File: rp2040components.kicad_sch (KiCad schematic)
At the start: 14 parts, among them P2 Header 1.27mm 2x5 PTH, P3 Header 3, U8 W25Q128JVSIQTR, Y1 X322512MSB4SI

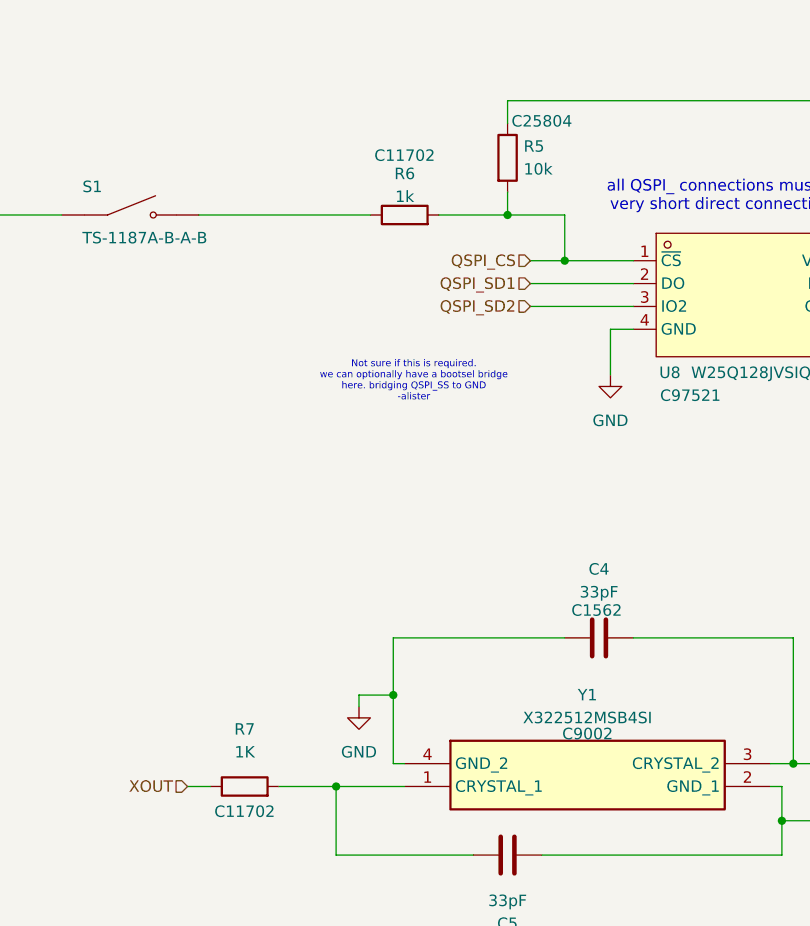
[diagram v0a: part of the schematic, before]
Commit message: Attached part number to components.
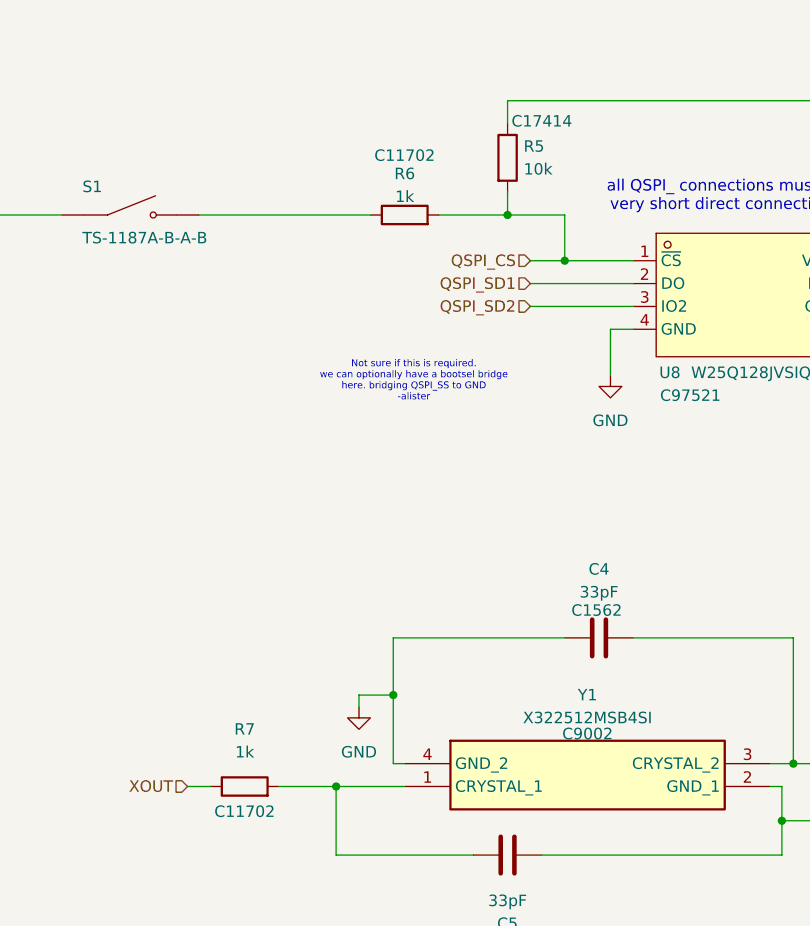
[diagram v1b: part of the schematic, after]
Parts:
- C18: value CL05B104KO5NNNC -> 100nF; footprint Imported Altium Library:CAPC1050X55X23ML05T13 -> Capacitor_SMD:C_0402_1005Metric
- R5: footprint Resistor_SMD:R_0603_1608Metric -> Resistor_SMD:R_0805_2012Metric; LCSC PN C25804 -> C17414
- R7: value 1K -> 1k
- Y1: footprint X322512MSB4SI -> Crystal:Crystal_SMD_TXC_7M-4Pin_3.2x2.5mm
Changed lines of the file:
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@@
 			)
 		)
-		(property "Footprint" "X322512MSB4SI"
+		(property "Footprint" "Crystal:Crystal_SMD_TXC_7M-4Pin_3.2x2.5mm"
 			(at 156.21 204.14 0)
 			(hide yes)
@@
 			)
 		)
-		(property "Footprint" "Resistor_SMD:R_0603_1608Metric"
+		(property "Footprint" "Resistor_SMD:R_0805_2012Metric"
 			(at 129.032 41.91 90)
 			(hide yes)
@@
 			)
 		)
-		(property "LCSC PN" "C25804"
+		(property "LCSC PN" "C17414"
 			(at 134.62 37.846 0)
 			(show_name no)
@@
 			)
 		)
-		(property "Value" "CL05B104KO5NNNC"
+		(property "Value" "100nF"
 			(at 259.08 127 0)
 			(hide yes)
@@
 			)
 		)
-		(property "Footprint" "Imported Altium Library:CAPC1050X55X23ML05T13"
+		(property "Footprint" "Capacitor_SMD:C_0402_1005Metric"
 			(at 255.27 119.38 0)
 			(hide yes)
@@
 			)
 		)
-		(property "Value" "1K"
+		(property "Value" "1k"
 			(at 101.6 107.95 90)
 			(show_name no)

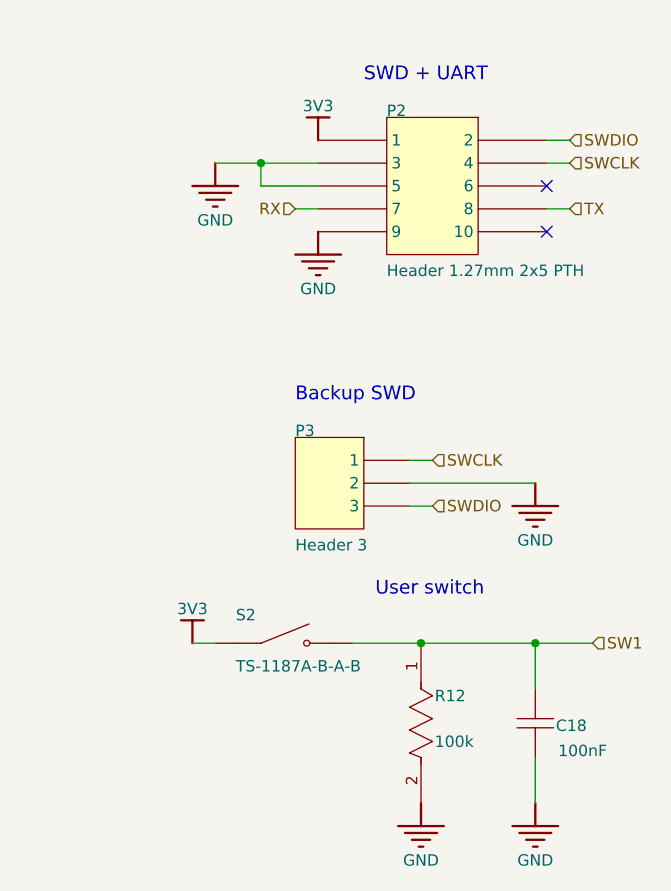
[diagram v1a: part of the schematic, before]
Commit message: Fix ERC errors.
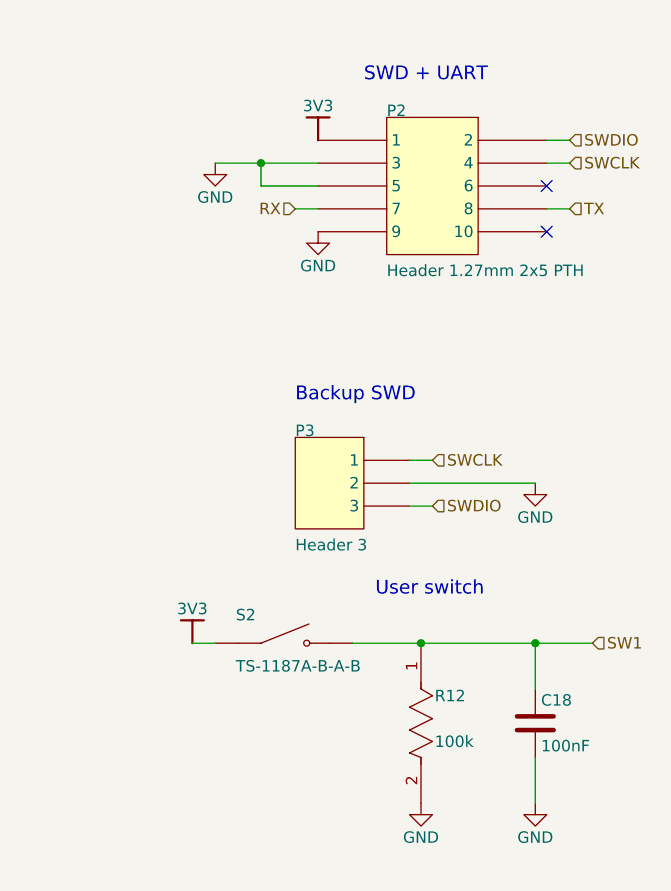
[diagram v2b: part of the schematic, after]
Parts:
- C18: symbol James Cook University:root_1_CAP-NP-2_James Cook University -> Device:C; CAPACITANCE 100nF -> (none); CASE SIZE/DIMENSION 0402 -> (none); DATASHEET URL https://datasheet.ciiva.com/29198/458718-da-01-en-vs-konden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 -> (none); DATASHEET VERSION Nov-10 -> (none); DIELECTRIC X7R -> (none); MANUFACTURER Samsung Electro-Mechanics -> (none); MANUFACTURER URL http://www.samsungsem.com/global/index.jsp -> (none); RATED VOLTAGE 16V -> (none); TOLERANCE (%) ±10% -> (none)
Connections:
- net GND: now also C18.2; no longer C18.1
- net SW1: now also C18.1; no longer C18.2

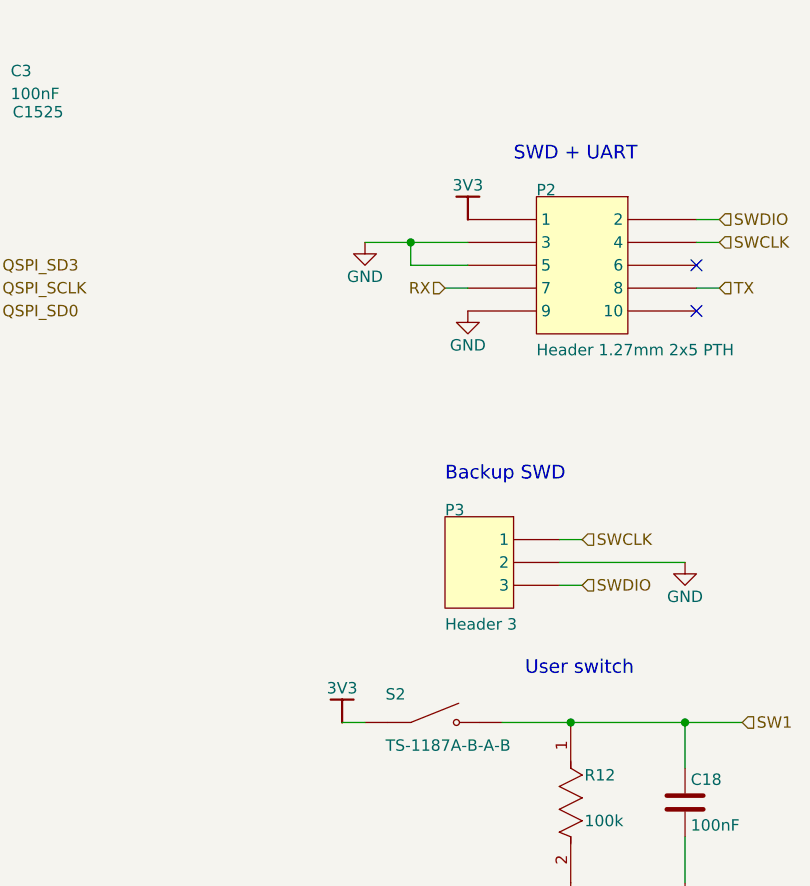
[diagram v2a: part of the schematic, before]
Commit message: Fix ERC errors.
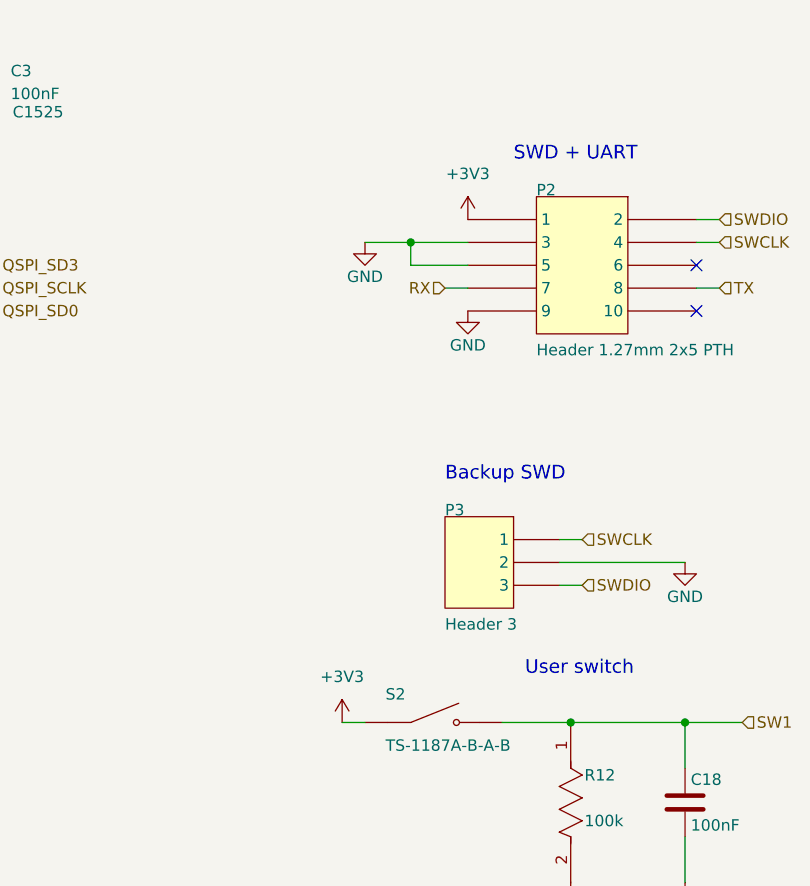
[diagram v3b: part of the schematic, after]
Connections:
- net 3V3 renamed +3V3
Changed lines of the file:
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@@
-	)
-	(symbol
-		(lib_id "CC3501 Assignment 1-altium-import:3V3_BAR")
-		(at 231.14 50.8 180)
-		(unit 1)
-		(body_style 1)
-		(exclude_from_sim no)
-		(in_bom yes)
-		(on_board yes)
-		(in_pos_files yes)
-		(dnp no)
-		(property "Reference" "#PWR0144"
-			(at 231.14 50.8 0)
-			(hide yes)
-			(show_name no)
-			(do_not_autoplace no)
-			(effects
-				(font
-					(size 1.27 1.27)
-				)
-			)
-		)
-		(property "Value" "3V3"
-			(at 231.14 46.99 0)
-			(show_name no)
-			(do_not_autoplace no)
-			(effects
-				(font
-					(size 1.27 1.27)
-				)
-			)
-		)
-		(property "Footprint" ""
-			(at 231.14 50.8 0)
-			(show_name no)
-			(do_not_autoplace no)
-			(effects
-				(font
-					(size 1.27 1.27)
-				)
-			)
-		)
-		(property "Datasheet" ""
-			(at 231.14 50.8 0)
-			(show_name no)
-			(do_not_autoplace no)
-			(effects
-				(font
-					(size 1.27 1.27)
-				)
-			)
-		)
-		(property "Description" ""
-			(at 231.14 50.8 0)
-			(show_name no)
-			(do_not_autoplace no)
-			(effects
-				(font
-					(size 1.27 1.27)
-				)
-			)
-		)
-		(pin ""
-		)
-		(instances
-			(project "CC3501-project-hardware"
-				(path "/4a2d49bb-8ba4-4c60-a8f0-05b8d2544445/bf94317a-9dda-4934-8bf5-bd19b681ec92"
-					(reference "#PWR0144")
-					(unit 1)
-				)
-			)
-		)
 	)
 	(symbol
@@
 	)
 	(symbol
+		(lib_id "power:+3V3")
+		(at 217.17 106.68 0)
+		(unit 1)
+		(body_style 1)
+		(exclude_from_sim no)
+		(in_bom yes)
+		(on_board yes)
+		(in_pos_files yes)
+		(dnp no)
+		(fields_autoplaced yes)
+		(property "Reference" "#PWR01"
+			(at 217.17 110.49 0)
+			(hide yes)
+			(show_name no)
+			(do_not_autoplace no)
+			(effects
+				(font
+					(size 1.27 1.27)
+				)
+			)
+		)
+		(property "Value" "+3V3"
+			(at 217.17 101.6 0)
+			(show_name no)
+			(do_not_autoplace no)
+			(effects
+				(font
+					(size 1.27 1.27)
+				)
+			)
+		)
+		(property "Footprint" ""
+			(at 217.17 106.68 0)
+			(hide yes)
+			(show_name no)
+			(do_not_autoplace no)
+			(effects
+				(font
+					(size 1.27 1.27)
+				)
+			)
+		)
+		(property "Datasheet" ""
+			(at 217.17 106.68 0)
+			(hide yes)
+			(show_name no)
+			(do_not_autoplace no)
+			(effects
+				(font
+					(size 1.27 1.27)
+				)
+			)
+		)
+		(property "Description" "Power symbol creates a global label with name \"+3V3\""
+			(at 217.17 106.68 0)
+			(hide yes)
+			(show_name no)
+			(do_not_autoplace no)
+			(effects
+				(font
+					(size 1.27 1.27)
+				)
+			)
+		)
+		(pin "1"
+		)
+		(instances
+			(project "CC3501-project-hardware"
+				(path "/4a2d49bb-8ba4-4c60-a8f0-05b8d2544445/bf94317a-9dda-4934-8bf5-bd19b681ec92"
+					(reference "#PWR01")
+					(unit 1)
+				)
+			)
+		)
+	)
+	(symbol
+		(lib_id "power:+3V3")
+		(at 231.14 50.8 0)
+		(unit 1)
+		(body_style 1)
+		(exclude_from_sim no)
+		(in_bom yes)
+		(on_board yes)
+		(in_pos_files yes)
+		(dnp no)
+		(fields_autoplaced yes)
+		(property "Reference" "#PWR076"
+			(at 231.14 54.61 0)
+			(hide yes)
+			(show_name no)
+			(do_not_autoplace no)
+			(effects
+				(font
+					(size 1.27 1.27)
+				)
+			)
+		)
+		(property "Value" "+3V3"
+			(at 231.14 45.72 0)
+			(show_name no)
+			(do_not_autoplace no)
+			(effects
+				(font
+					(size 1.27 1.27)
+				)
+			)
+		)
+		(property "Footprint" ""
+			(at 231.14 50.8 0)
+			(hide yes)
+			(show_name no)
+			(do_not_autoplace no)
+			(effects
+				(font
+					(size 1.27 1.27)
+				)
+			)
+		)
+		(property "Datasheet" ""
+			(at 231.14 50.8 0)
+			(hide yes)
+			(show_name no)
+			(do_not_autoplace no)
+			(effects
+				(font
+					(size 1.27 1.27)
+				)
+			)
+		)
+		(property "Description" "Power symbol creates a global label with name \"+3V3\""
+			(at 231.14 50.8 0)
+			(hide yes)
+			(show_name no)
+			(do_not_autoplace no)
+			(effects
+				(font
+					(size 1.27 1.27)
+				)
+			)
+		)
+		(pin "1"
+		)
+		(instances
+			(project "CC3501-project-hardware"
+				(path "/4a2d49bb-8ba4-4c60-a8f0-05b8d2544445/bf94317a-9dda-4934-8bf5-bd19b681ec92"
+					(reference "#PWR076")
+					(unit 1)
+				)
+			)
+		)
+	)
+	(symbol
 		(lib_id "power:GND")
 		(at 176.53 40.64 0)
@@
 					(unit 1)
 				)
-			)
-		)
-	)
-	(symbol
-		(lib_id "CC3501 Assignment 1-altium-import:3V3_BAR")
-		(at 217.17 106.68 180)
-		(unit 1)
-		(body_style 1)
-		(exclude_from_sim no)
-		(in_bom yes)
-		(on_board yes)
-		(in_pos_files yes)
-		(dnp no)
-		(property "Reference" "#PWR0143"
-			(at 217.17 106.68 0)
-			(hide yes)
-			(show_name no)
-			(do_not_autoplace no)
-			(effects
-				(font
-					(size 1.27 1.27)
-				)
-			)
-		)
-		(property "Value" "3V3"
-			(at 217.17 102.87 0)
-			(show_name no)
-			(do_not_autoplace no)
-			(effects
-				(font
-					(size 1.27 1.27)
-				)
-			)
-		)
-		(property "Footprint" ""
-			(at 217.17 106.68 0)
-			(show_name no)
-			(do_not_autoplace no)
-			(effects
-				(font
-					(size 1.27 1.27)
-				)
-			)
-		)
-		(property "Datasheet" ""
-			(at 217.17 106.68 0)
-			(show_name no)
-			(do_not_autoplace no)
-			(effects
-				(font
-					(size 1.27 1.27)
-				)
-			)
-		)
-		(property "Description" ""
-			(at 217.17 106.68 0)
-			(show_name no)
-			(do_not_autoplace no)
-			(effects
-				(font
-					(size 1.27 1.27)
-				)
-			)
-		)
-		(pin ""
-		)
-		(instances
-			(project "CC3501-project-hardware"
-				(path "/4a2d49bb-8ba4-4c60-a8f0-05b8d2544445/bf94317a-9dda-4934-8bf5-bd19b681ec92"
-					(reference "#PWR0143")
-					(unit 1)
-				)

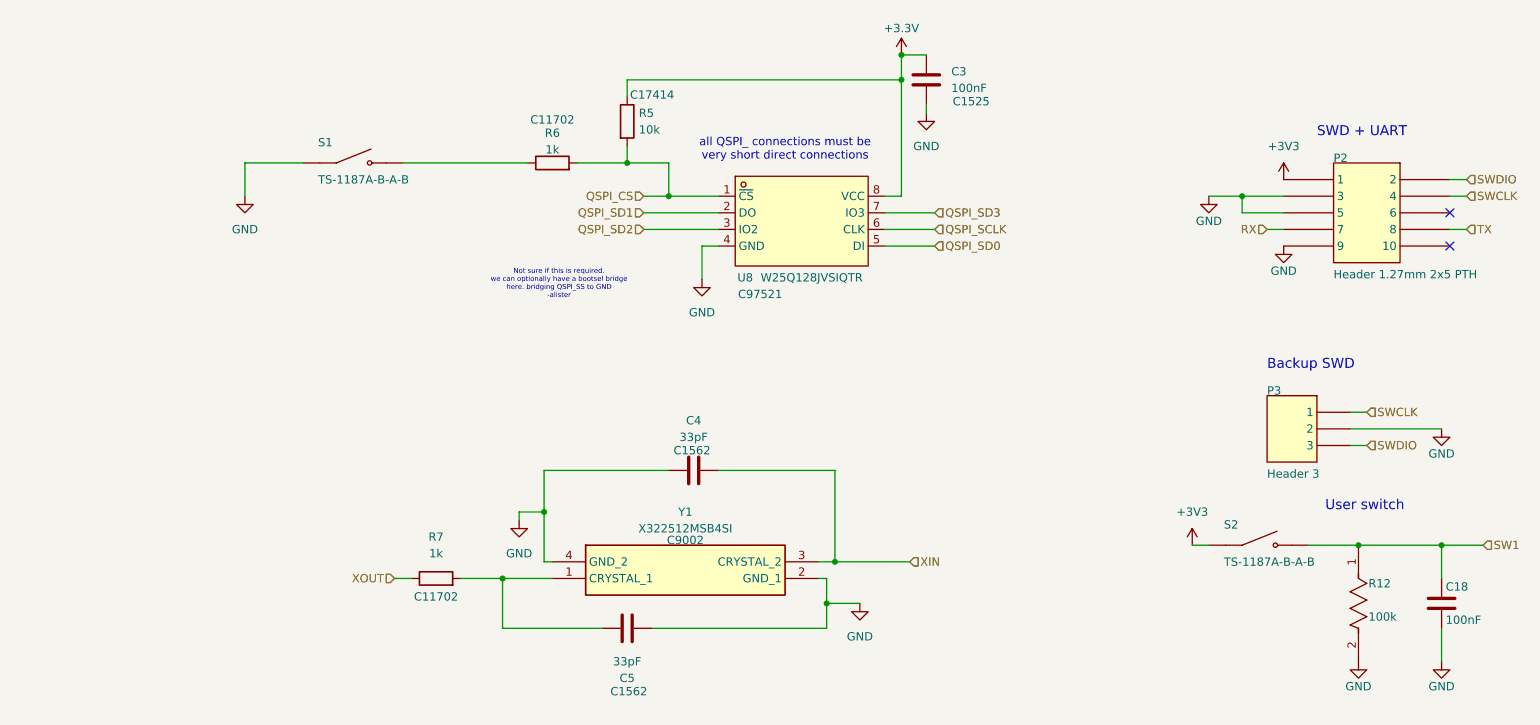
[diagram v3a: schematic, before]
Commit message: Remove duplicated power flag.
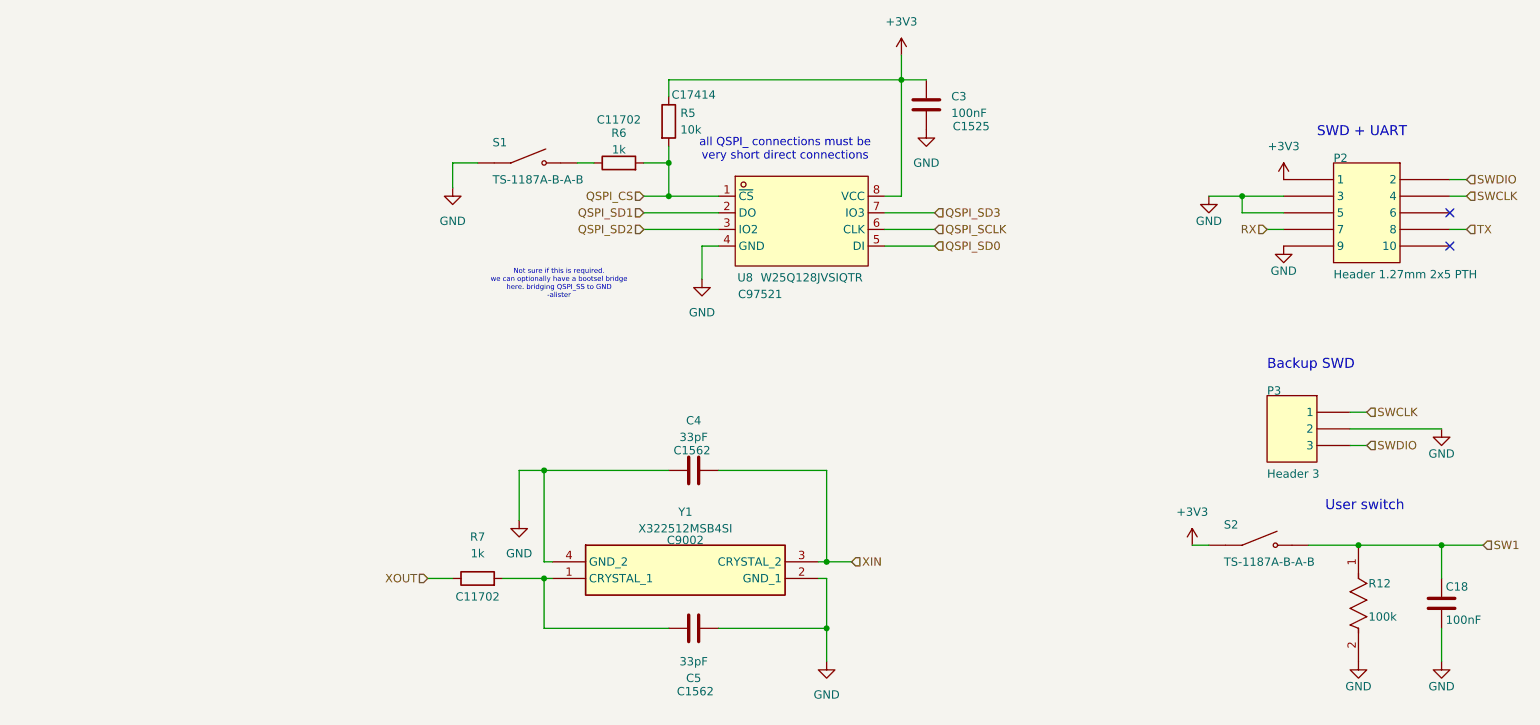
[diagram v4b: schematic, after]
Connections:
- net +3.3V is gone; now on net +3V3: C3.1, R5.1, U8.8 (VCC)
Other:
- moved on the sheet: C3, C5, R5, R6, R7, S1

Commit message: edit HX711 configuration to match datasheet and sparkfun example as well as add JLC part numbers and display them on schematic
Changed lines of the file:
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@@
 		)
 		(property "LCSC PN" "C25803"
-			(at 242.57 106.68 0)
-			(hide yes)
+			(at 247.65 115.062 0)
 			(show_name no)
 			(do_not_autoplace no)
@@
 		)
 		(property "LCSC PN" "C318884"
-			(at 227.33 106.68 0)
-			(hide yes)
+			(at 228.092 111.252 0)
 			(show_name no)
 			(do_not_autoplace no)
@@
 		)
 		(property "LCSC PN" "C1525"
-			(at 255.27 115.57 0)
-			(hide yes)
+			(at 258.826 120.142 0)
 			(show_name no)
 			(do_not_autoplace no)
@@
 		)
 		(property "LCSC PN" "C318884"
-			(at 115.57 48.26 0)
-			(hide yes)
+			(at 115.062 53.086 0)
 			(show_name no)
 			(do_not_autoplace no)

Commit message: Add reset switch to RUN pin.
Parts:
- added R18: 10k, Resistor_SMD:R_0805_2012Metric, symbol Device:R
- added S3: TS-1187A-B-A-B, Button_Switch_SMD:SW_Push_1P1T_XKB_TS-1187A, symbol James Cook University:root_0_TS-1187A-B-A-B_James Cook University
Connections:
- net +3V3: now also R18.1
- net GND: now also S3.A (COM), S3.B (COM)
- new net RUN: R18.2, S3.C (NO), S3.D (NO)
